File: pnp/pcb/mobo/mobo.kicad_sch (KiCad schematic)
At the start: 0 parts

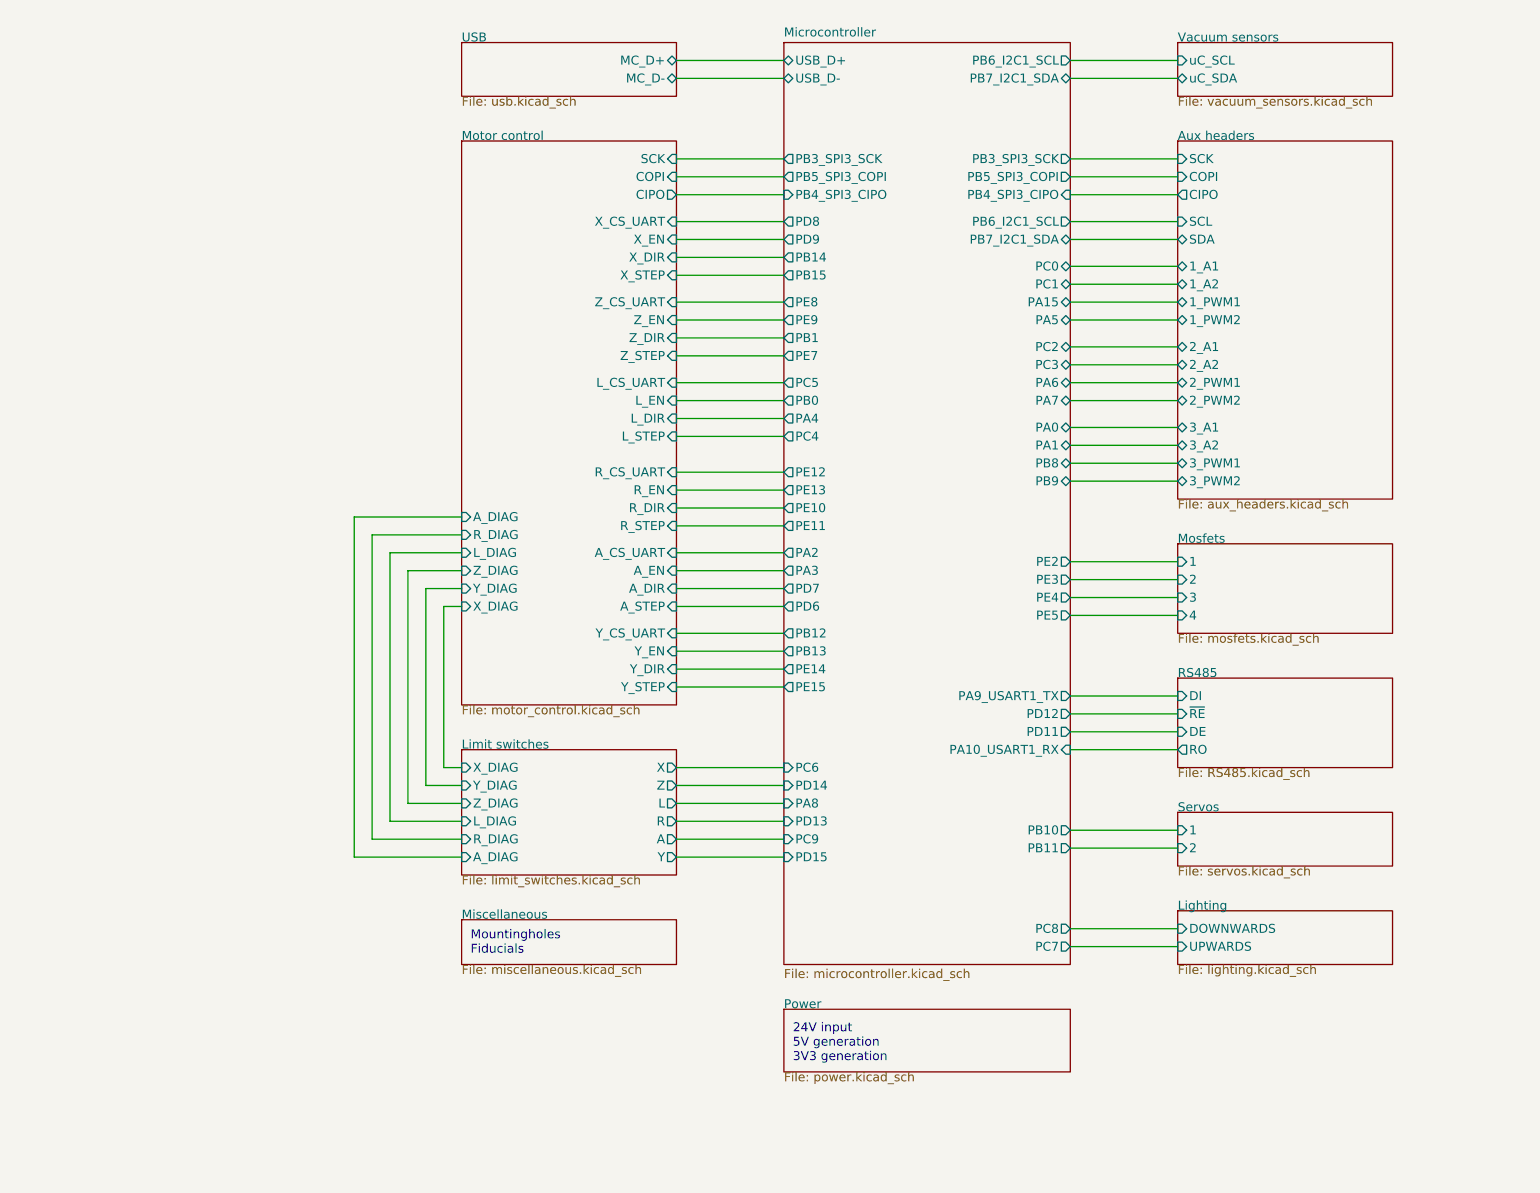
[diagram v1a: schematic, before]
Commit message: Replaced solder jumpers with 0ohm
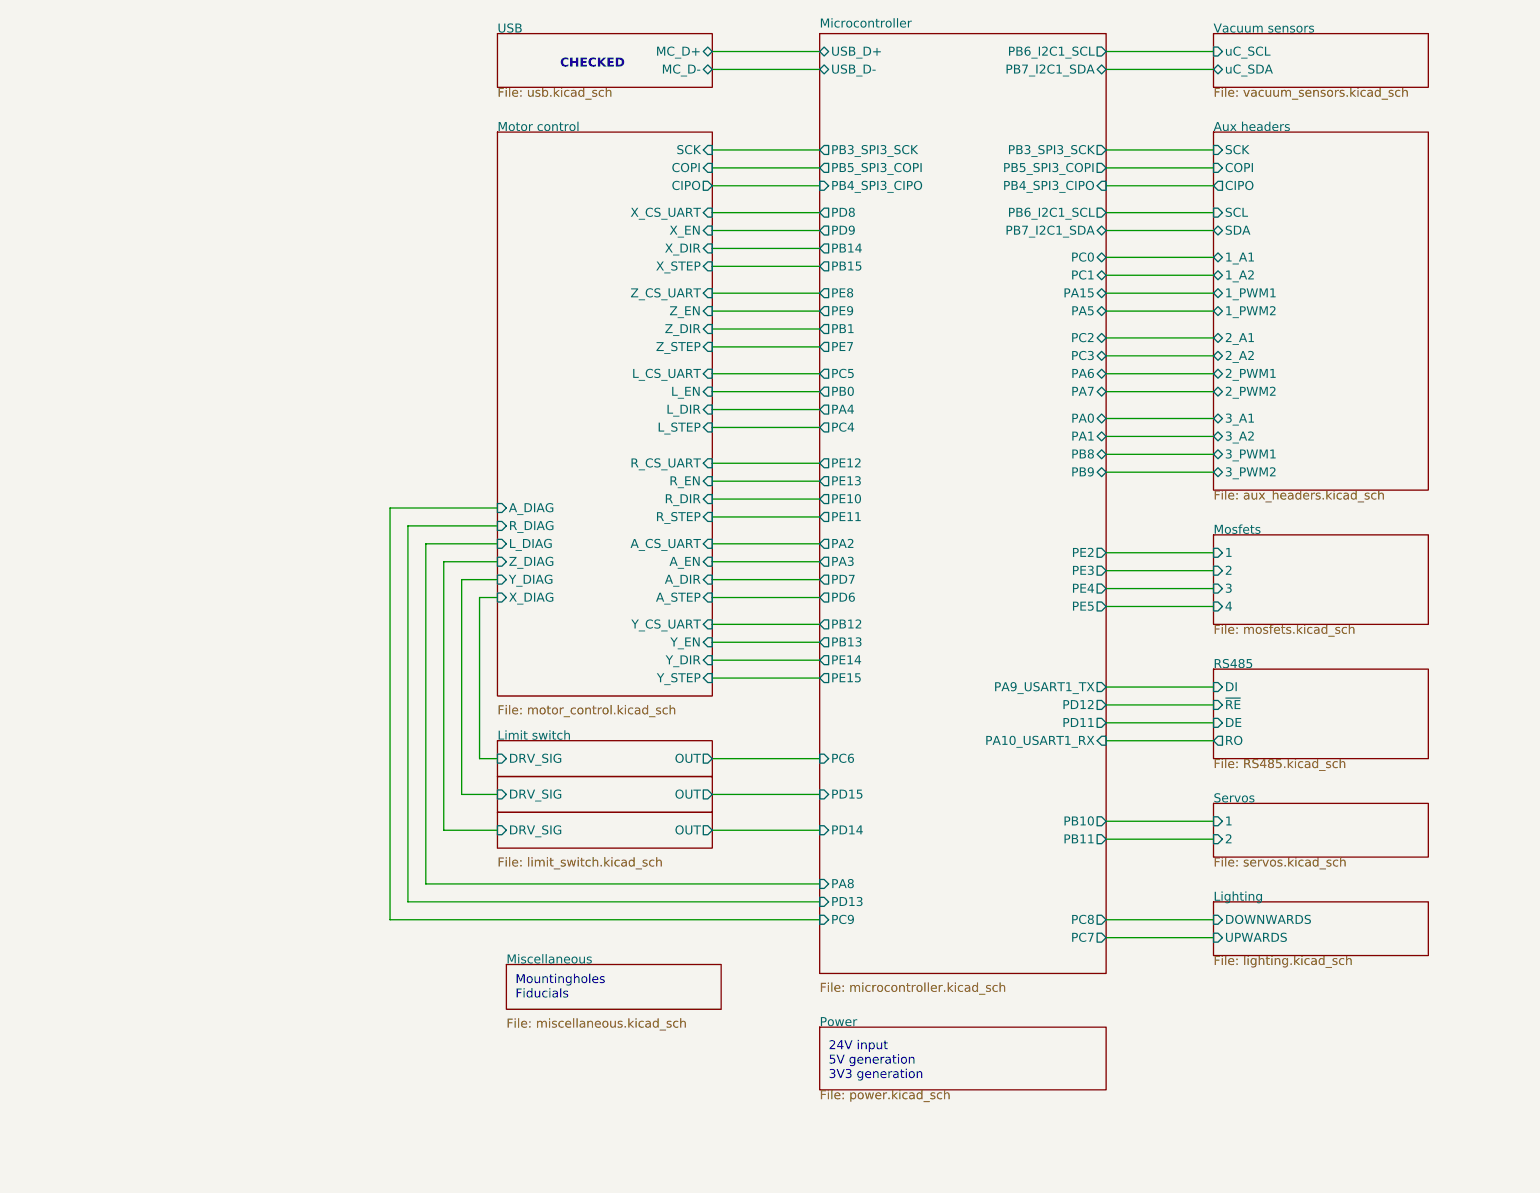
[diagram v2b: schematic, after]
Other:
- sheet Limit switches renamed Limit switch
- added sheet Limit switch1 (limit_switch.kicad_sch)
- added sheet Limit switch2 (limit_switch.kicad_sch)
- sheet Limit switch: file limit_switches.kicad_sch -> limit_switch.kicad_sch
- sheet Limit switch ports: added DRV_SIG, OUT; removed A, A_DIAG, L, L_DIAG, R, R_DIAG, X, X_DIAG, Y, Y_DIAG, Z, Z_DIAG
- note added: "CHECKED"

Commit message: Motor driver new Symbol and fix TVS placement
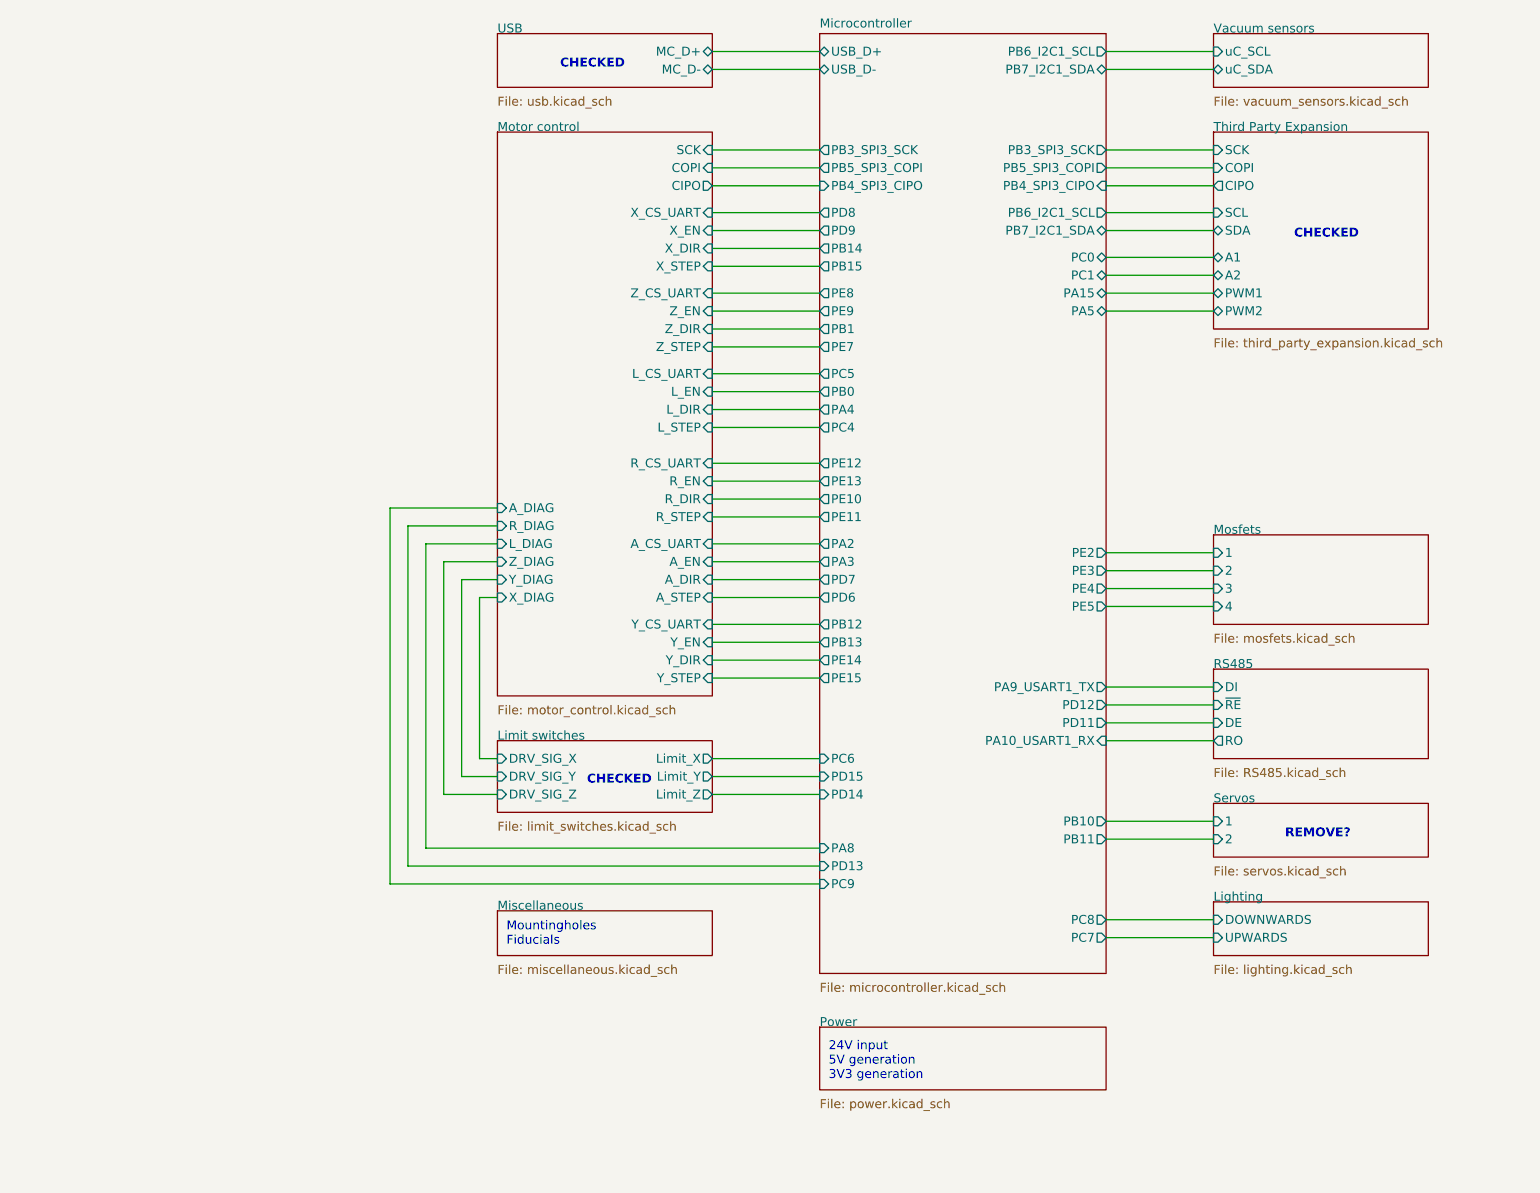
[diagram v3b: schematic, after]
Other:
- sheet Aux headers renamed Third Party Expansion
- sheet Limit switch2 renamed Limit switches
- removed sheet Limit switch
- removed sheet Limit switch1
- sheet Limit switches: file limit_switch.kicad_sch -> limit_switches.kicad_sch
- sheet Limit switches ports: added DRV_SIG_X, DRV_SIG_Y, DRV_SIG_Z, Limit_X, Limit_Y, Limit_Z; removed DRV_SIG, OUT
- sheet Microcontroller ports: added none; removed PA0, PA1, PA6, PA7, PB8, PB9, PC2, PC3
- sheet Third Party Expansion: file aux_headers.kicad_sch -> third_party_expansion.kicad_sch
- sheet Third Party Expansion ports: added A1, A2, PWM1, PWM2; removed 1_A1, 1_A2, 1_PWM1, 1_PWM2, 2_A1, 2_A2, 2_PWM1, 2_PWM2, 3_A1, 3_A2, 3_PWM1, 3_PWM2
- note added: "REMOVE?"

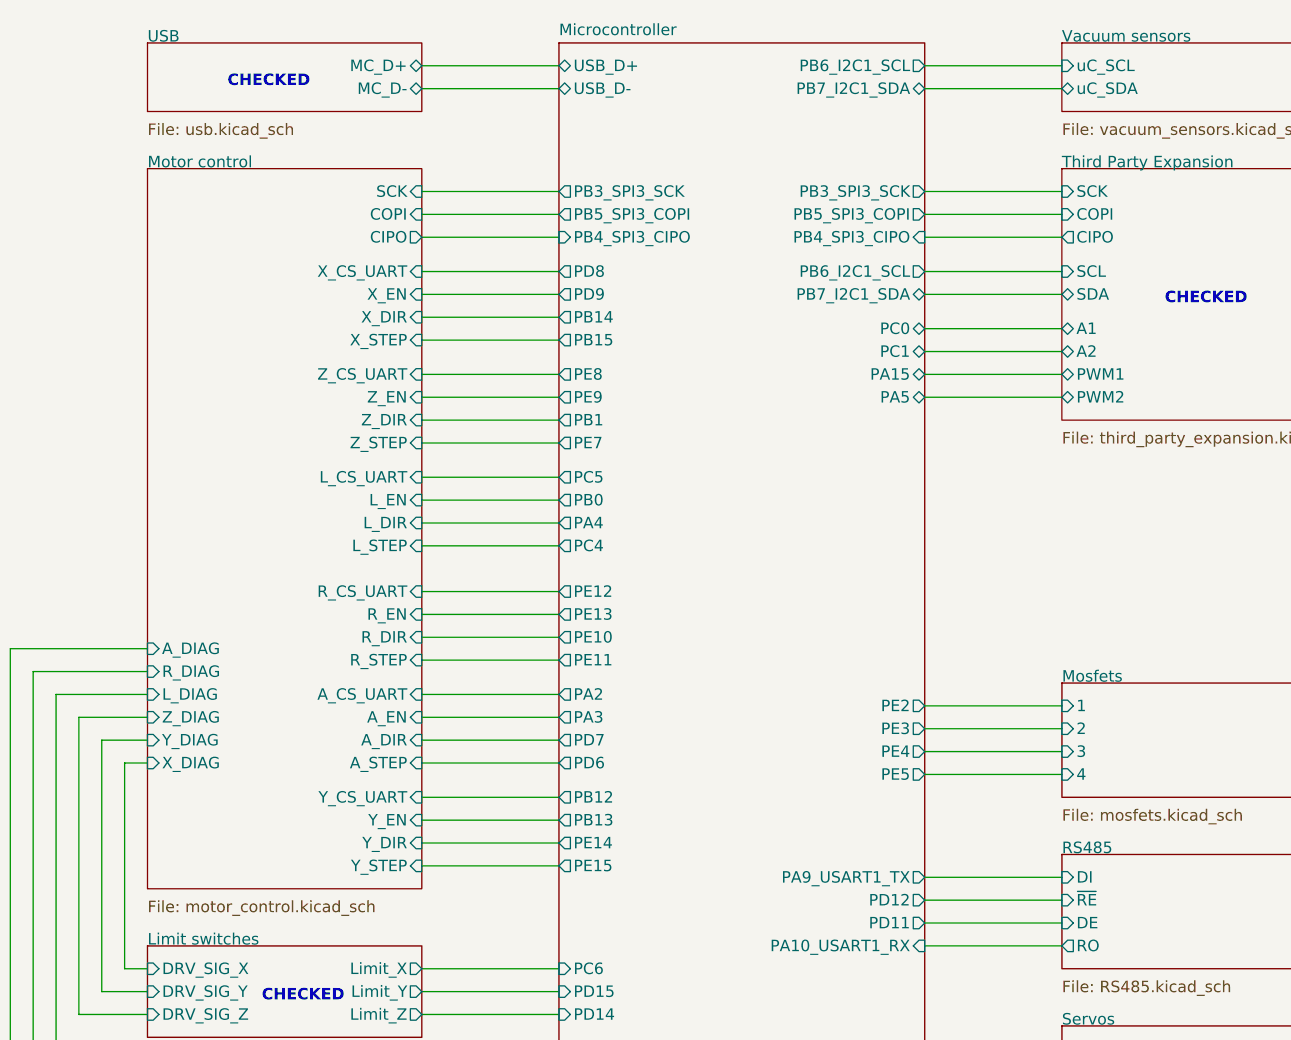
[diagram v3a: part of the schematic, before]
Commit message: Increased motor driver sense resistor package size
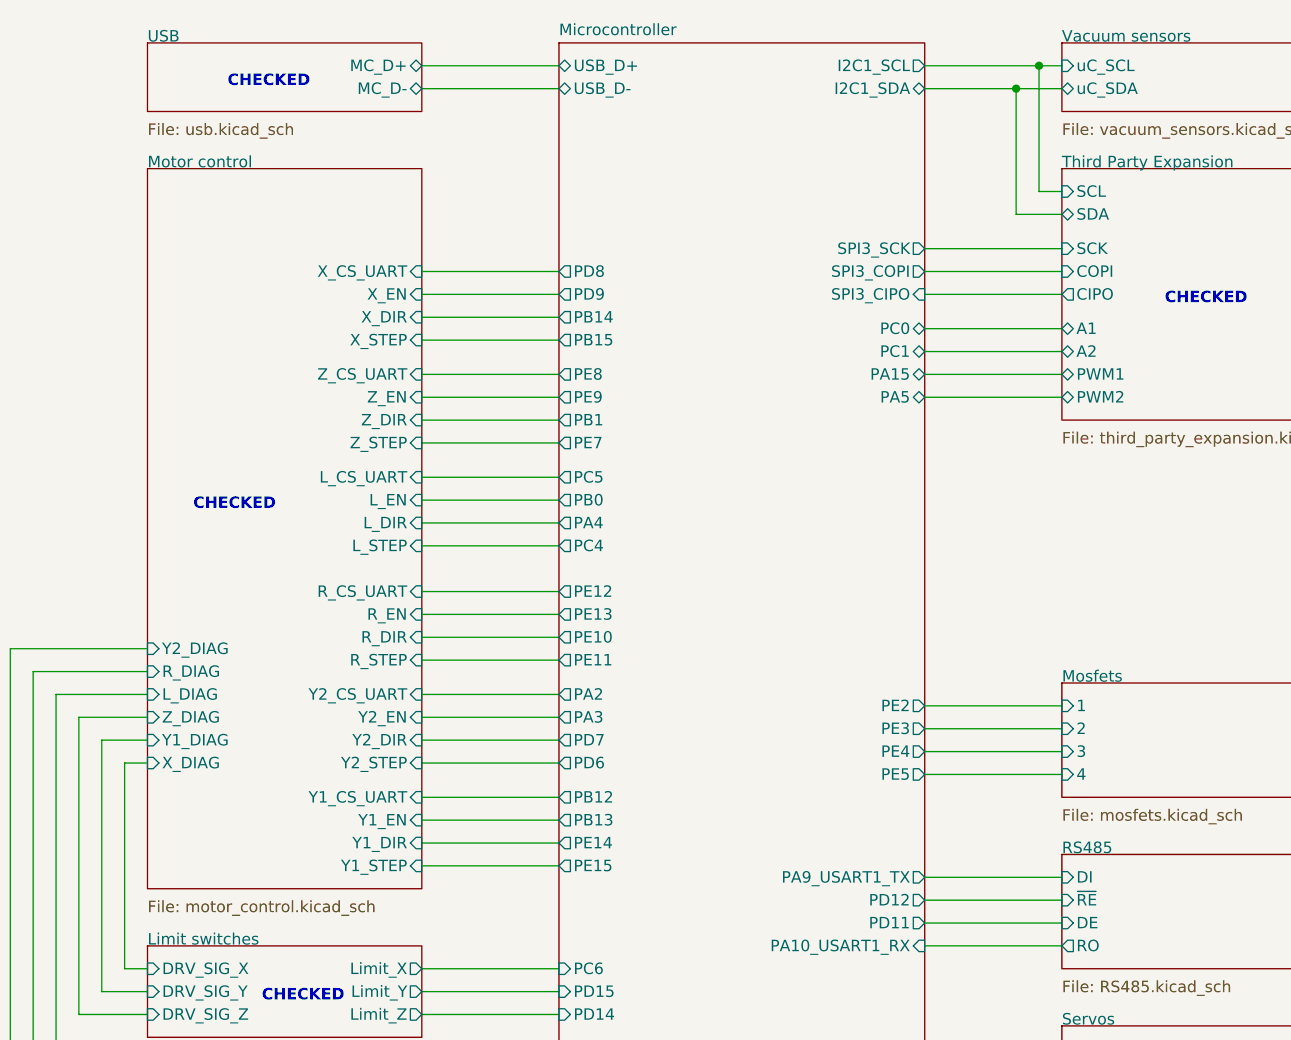
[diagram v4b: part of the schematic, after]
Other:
- sheet Microcontroller ports: added I2C1_SCL, I2C1_SDA, SPI3_CIPO, SPI3_COPI, SPI3_SCK; removed PB3_SPI3_SCK, PB4_SPI3_CIPO, PB5_SPI3_COPI, PB6_I2C1_SCL, PB7_I2C1_SDA
- sheet Motor control ports: added Y1_CS_UART, Y1_DIAG, Y1_DIR, Y1_EN, Y1_STEP, Y2_CS_UART, Y2_DIAG, Y2_DIR, Y2_EN, Y2_STEP; removed A_CS_UART, A_DIAG, A_DIR, A_EN, A_STEP, CIPO, COPI, SCK, Y_CS_UART, Y_DIAG, Y_DIR, Y_EN, Y_STEP

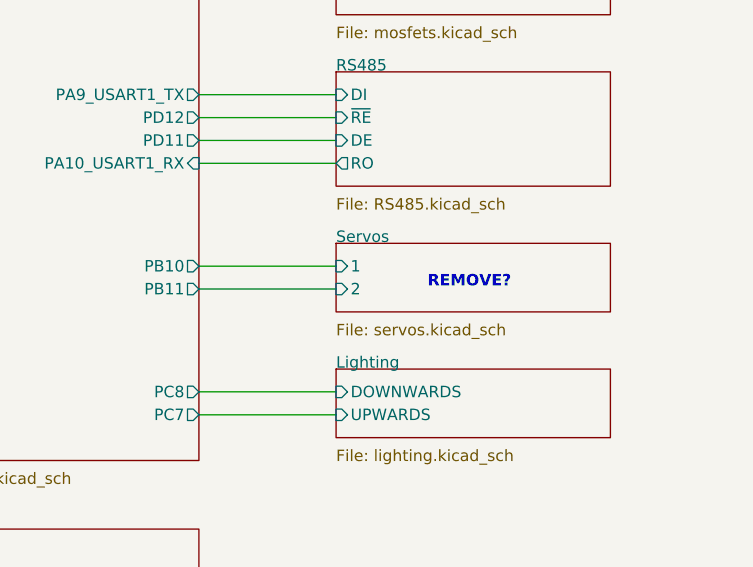
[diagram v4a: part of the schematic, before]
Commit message: Removed Servos and added test points
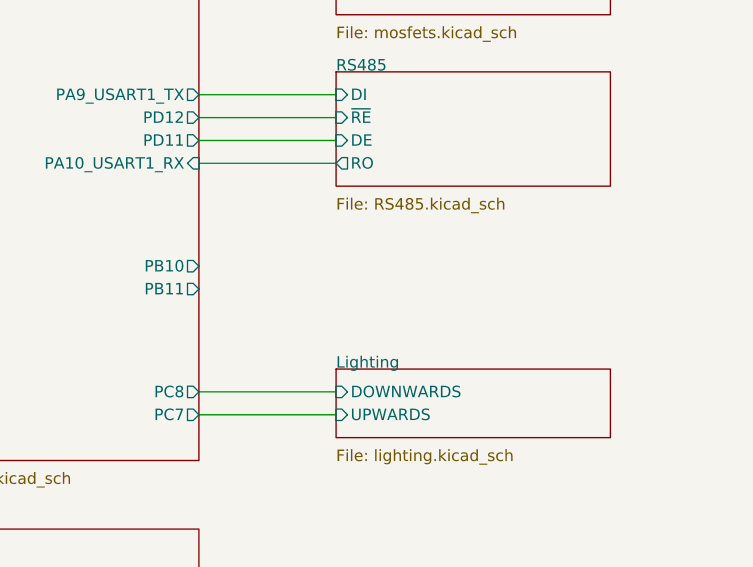
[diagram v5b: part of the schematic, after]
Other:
- removed sheet Servos
- note removed: "REMOVE?"
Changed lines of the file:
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@@
-    (stroke (width 0) (type default))
-  )
-  (wire (pts (xy 171.45 140.97) (xy 186.69 140.97))
     (stroke (width 0) (type default))
   )
@@
   )
   (wire (pts (xy 171.45 31.75) (xy 184.15 31.75))
-    (stroke (width 0) (type default))
-  )
-  (wire (pts (xy 171.45 143.51) (xy 186.69 143.51))
     (stroke (width 0) (type default))
   )
@@
     (effects (font (size 1.27 1.27) (thickness 0.254) bold (color 0 127 0 1)) (justify left bottom))
   )
-  (text "REMOVE?" (at 196.85 143.51 0)
-    (effects (font (size 1.27 1.27) (thickness 0.254) bold (color 255 0 0 1)) (justify left bottom))
-  )
   (text "CHECKED" (at 90.17 81.28 0)
     (effects (font (size 1.27 1.27) (thickness 0.254) bold (color 0 127 0 1)) (justify left bottom))
@@
       )
     )
-  )
-  (sheet (at 186.69 138.43) (size 30.48 7.62)
-    (stroke (width 0.1524) (type solid))
-    (fill (color 0 0 0 0.0000))
-    (property "Sheetname" "Servos" (at 186.69 138.43 0)
-      (effects (font (size 1.27 1.27)) (justify left bottom))
-    )
-    (property "Sheetfile" "servos.kicad_sch" (at 186.69 147.32 0)
-      (effects (font (size 1.27 1.27)) (justify left top))
-    )
-    (pin "1" input (at 186.69 140.97 180)
-      (effects (font (size 1.27 1.27)) (justify left))
-    )
-    (pin "2" input (at 186.69 143.51 180)
-      (effects (font (size 1.27 1.27)) (justify left))
-    )
-    (instances
-      (project "mobo"
-        (path "/7255cbd1-8d38-4545-be9a-7fc5488ef942" (page "22"))
-      )
-    )
